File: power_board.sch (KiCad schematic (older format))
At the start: 27 parts, among them CON1 MICROUSB, J1 Conn_02x03_Odd_Even, J2 Conn_01x01, J3 Conn_01x01, J4 Conn_01x01, J5 Conn_01x01, SW1 SW_Push, U1 PCA9555PW, U2 ATMEGA328P-AU, U3 PCA9555PW, U4 FT232RL, Y1 Crystal

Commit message: Start MCU layout
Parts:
- added C1, C5, C6, C7, C9: 100nF, lsts-passives:C_0603, symbol Device:C
- renumbered C5 to C10, C1 to C2, C2 to C3, C3 to C4, C4 to C8
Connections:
- net +5V_SB: now also C1.2, C5.1, C6.1, C7.2
- net 5V_USB: now also C9.2
- net GND: now also C1.1, C5.2, C6.2, C7.1, C9.1
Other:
- moved on the sheet: C2, C8
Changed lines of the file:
@@
 	9550 3250 9450 3250
 $Comp
-L power:GND #PWR014
+L power:GND #PWR016
 U 1 1 5DC0D5DB
 P 9250 3400
-F 0 "#PWR014" H 9250 3150 50  0001 C CNN
+F 0 "#PWR016" H 9250 3150 50  0001 C CNN
 F 1 "GND" V 9255 3272 50  0000 R CNN
 F 2 "" H 9250 3400 50  0001 C CNN
@@
 	7650 1900 7800 1900
 $Comp
-L power:GND #PWR011
+L power:GND #PWR014
 U 1 1 5DC4811C
 P 7800 1300
-F 0 "#PWR011" H 7800 1050 50  0001 C CNN
+F 0 "#PWR014" H 7800 1050 50  0001 C CNN
 F 1 "GND" H 7805 1127 50  0000 C CNN
 F 2 "" H 7800 1300 50  0001 C CNN
@@
 	3750 1450 3600 1450
 $Comp
-L power:GND #PWR09
+L power:GND #PWR010
 U 1 1 5DC9272C
 P 4400 1550
-F 0 "#PWR09" H 4400 1300 50  0001 C CNN
+F 0 "#PWR010" H 4400 1300 50  0001 C CNN
 F 1 "GND" H 4405 1377 50  0000 C CNN
 F 2 "" H 4400 1550 50  0001 C CNN
@@
 MOSI
 $Comp
-L Device:C C4
+L Device:C C8
 U 1 1 5DCA5008
-P 7800 2200
-F 0 "C4" H 7915 2246 50  0000 L CNN
-F 1 "100nF" H 7915 2155 50  0000 L CNN
-F 2 "lsts-passives:C_0603" H 7838 2050 50  0001 C CNN
-F 3 "~" H 7800 2200 50  0001 C CNN
-	1    7800 2200
-	-1   0    0    1
-$EndComp
-$Comp
-L power:GND #PWR012
-U 1 1 5DCA65D2
-P 7800 2500
-F 0 "#PWR012" H 7800 2250 50  0001 C CNN
-F 1 "GND" H 7805 2327 50  0000 C CNN
-F 2 "" H 7800 2500 50  0001 C CNN
-F 3 "" H 7800 2500 50  0001 C CNN
-	1    7800 2500
-	1    0    0    -1
+P 7400 2700
+F 0 "C8" H 7515 2746 50  0000 L CNN
+F 1 "100nF" H 7515 2655 50  0000 L CNN
+F 2 "lsts-passives:C_0603" H 7438 2550 50  0001 C CNN
+F 3 "~" H 7400 2700 50  0001 C CNN
+	1    7400 2700
+	-1   0    0    1
 $EndComp
 Wire Wire Line
@@
 NoConn ~ 10250 2800
 $Comp
-L power:GND #PWR02
+L power:GND #PWR01
 U 1 1 5DC3EC2B
 P 950 3950
-F 0 "#PWR02" H 950 3700 50  0001 C CNN
+F 0 "#PWR01" H 950 3700 50  0001 C CNN
 F 1 "GND" H 955 3777 50  0000 C CNN
 F 2 "" H 950 3950 50  0001 C CNN
@@
 	3250 850  3400 850
 $Comp
-L Device:C C1
+L Device:C C2
 U 1 1 5DC4BEF5
-P 950 1100
-F 0 "C1" V 698 1100 50  0000 C CNN
-F 1 "100nF" V 789 1100 50  0000 C CNN
-F 2 "lsts-passives:C_0603" H 988 950 50  0001 C CNN
-F 3 "~" H 950 1100 50  0001 C CNN
-	1    950  1100
-	-1   0    0    1
-$EndComp
-$Comp
-L power:GND #PWR01
-U 1 1 5DC4DED9
-P 950 800
-F 0 "#PWR01" H 950 550 50  0001 C CNN
-F 1 "GND" V 955 672 50  0000 R CNN
-F 2 "" H 950 800 50  0001 C CNN
-F 3 "" H 950 800 50  0001 C CNN
-	1    950  800
-	-1   0    0    1
+P 3750 3200
+F 0 "C2" V 3498 3200 50  0000 C CNN
+F 1 "100nF" V 3589 3200 50  0000 C CNN
+F 2 "lsts-passives:C_0603" H 3788 3050 50  0001 C CNN
+F 3 "~" H 3750 3200 50  0001 C CNN
+	1    3750 3200
+	1    0    0    -1
 $EndComp
 Wire Wire Line
@@
 	2300 850  2150 850
 $Comp
-L power:GND #PWR04
+L power:GND #PWR03
 U 1 1 5DC6E12C
 P 2150 850
-F 0 "#PWR04" H 2150 600 50  0001 C CNN
+F 0 "#PWR03" H 2150 600 50  0001 C CNN
 F 1 "GND" H 2155 677 50  0000 C CNN
 F 2 "" H 2150 850 50  0001 C CNN
@@
 $EndComp
 $Comp
-L Device:C C2
+L Device:C C3
 U 1 1 5DC9A9C9
 P 3800 2000
-F 0 "C2" V 3548 2000 50  0000 C CNN
+F 0 "C3" V 3548 2000 50  0000 C CNN
 F 1 "22nF" V 3639 2000 50  0000 C CNN
 F 2 "lsts-passives:C_0603" H 3838 1850 50  0001 C CNN
@@
 $EndComp
 $Comp
-L Device:C C3
+L Device:C C4
 U 1 1 5DC9B617
 P 3800 2300
-F 0 "C3" V 3960 2300 50  0000 C CNN
+F 0 "C4" V 3960 2300 50  0000 C CNN
 F 1 "22nF" V 4051 2300 50  0000 C CNN
 F 2 "lsts-passives:C_0603" H 3838 2150 50  0001 C CNN
@@
 Wire Wire Line
 	3950 2300 4150 2300
-Text Label 800  1350 2    50   ~ 0
+Text Label 950  1200 1    50   ~ 0
 +5V_SB
-Wire Wire Line
-	950  950  950  800
-Wire Wire Line
-	950  1350 800  1350
-Connection ~ 950  1350
-Wire Wire Line
-	950  1350 950  1250
 $Comp
 L lsts-conn:MICROUSB CON1
@@
 	1750 7050 1750 7150
 $Comp
-L power:GND #PWR03
+L power:GND #PWR02
 U 1 1 5E1B9B28
 P 1750 7150
-F 0 "#PWR03" H 1750 6900 50  0001 C CNN
+F 0 "#PWR02" H 1750 6900 50  0001 C CNN
 F 1 "GND" H 1755 6977 50  0000 C CNN
 F 2 "" H 1750 7150 50  0001 C CNN
@@
 	4250 7050 4250 7150
 $Comp
-L power:GND #PWR08
+L power:GND #PWR09
 U 1 1 5E1C2465
 P 4250 7150
-F 0 "#PWR08" H 4250 6900 50  0001 C CNN
+F 0 "#PWR09" H 4250 6900 50  0001 C CNN
 F 1 "GND" H 4255 6977 50  0000 C CNN
 F 2 "" H 4250 7150 50  0001 C CNN
@@
 	9350 1100 9350 950
 $Comp
-L power:GND #PWR013
+L power:GND #PWR015
 U 1 1 5DC6C013
 P 8550 750
-F 0 "#PWR013" H 8550 500 50  0001 C CNN
+F 0 "#PWR015" H 8550 500 50  0001 C CNN
 F 1 "GND" H 8555 577 50  0000 C CNN
 F 2 "" H 8550 750 50  0001 C CNN
@@
 	8650 1400 8550 1400
 $Comp
-L Device:C C5
+L Device:C C10
 U 1 1 5DC6AA97
 P 8550 1100
-F 0 "C5" H 8665 1146 50  0000 L CNN
+F 0 "C10" H 8665 1146 50  0000 L CNN
 F 1 "100nF" H 8665 1055 50  0000 L CNN
 F 2 "lsts-passives:C_0603" H 8588 950 50  0001 C CNN
@@
 Text Label 4400 1250 0    50   ~ 0
 +5V_SB
-Wire Wire Line
-	7800 1900 7800 2050
-Wire Wire Line
-	7800 2350 7800 2500
 Text Label 7800 1900 0    50   ~ 0
 5V_USB
@@
 $EndComp
 $Comp
-L power:GND #PWR010
+L power:GND #PWR012
 U 1 1 5E29E574
 P 6700 7500
-F 0 "#PWR010" H 6700 7250 50  0001 C CNN
+F 0 "#PWR012" H 6700 7250 50  0001 C CNN
 F 1 "GND" H 6705 7327 50  0000 C CNN
 F 2 "" H 6700 7500 50  0001 C CNN
@@
 	950  3600 950  3700
 Connection ~ 950  3700
-Wire Wire Line
-	950  1500 950  1350
 Wire Wire Line
 	950  1600 950  1500
@@
 NoConn ~ 4750 6700
 NoConn ~ 4750 6800
+Wire Wire Line
+	950  1200 950  1500
+$Comp
+L Device:C C5
+U 1 1 5E48DB47
+P 4150 3200
+F 0 "C5" V 3898 3200 50  0000 C CNN
+F 1 "100nF" V 3989 3200 50  0000 C CNN
+F 2 "lsts-passives:C_0603" H 4188 3050 50  0001 C CNN
+F 3 "~" H 4150 3200 50  0001 C CNN
+	1    4150 3200
+	1    0    0    -1
+$EndComp
+$Comp
+L power:GND #PWR08
+U 1 1 5E48DB4D
+P 4150 3500
+F 0 "#PWR08" H 4150 3250 50  0001 C CNN
+F 1 "GND" V 4155 3372 50  0000 R CNN
+F 2 "" H 4150 3500 50  0001 C CNN
+F 3 "" H 4150 3500 50  0001 C CNN
+	1    4150 3500
+	1    0    0    -1
+$EndComp
+Wire Wire Line
+	4150 3350 4150 3500
+Wire Wire Line
+	4150 2900 4150 3050
+$Comp
+L Device:C C6
+U 1 1 5E499A74
+P 4550 3200
+F 0 "C6" V 4298 3200 50  0000 C CNN
+F 1 "100nF" V 4389 3200 50  0000 C CNN
+F 2 "lsts-passives:C_0603" H 4588 3050 50  0001 C CNN
+F 3 "~" H 4550 3200 50  0001 C CNN
+	1    4550 3200
+	1    0    0    -1
+$EndComp
+Wire Wire Line
+	3750 3350 4150 3350
+Connection ~ 4150 3350
+Wire Wire Line
+	4150 3350 4550 3350
+Wire Wire Line
+	3750 3050 4150 3050
+Connection ~ 4150 3050
+Wire Wire Line
+	4150 3050 4550 3050
+Text Label 4150 2900 1    50   ~ 0
++5V_SB
+$Comp
+L Device:C C9
+U 1 1 5E51421A
+P 7800 2700
+F 0 "C9" H 7685 2654 50  0000 R CNN
+F 1 "100nF" H 7685 2745 50  0000 R CNN
+F 2 "lsts-passives:C_0603" H 7838 2550 50  0001 C CNN
+F 3 "~" H 7800 2700 50  0001 C CNN
+	1    7800 2700
+	-1   0    0    1
+$EndComp
+$Comp
+L power:GND #PWR013
+U 1 1 5E514220
+P 7600 3000
+F 0 "#PWR013" H 7600 2750 50  0001 C CNN
+F 1 "GND" H 7605 2827 50  0000 C CNN
+F 2 "" H 7600 3000 50  0001 C CNN
+F 3 "" H 7600 3000 50  0001 C CNN
+	1    7600 3000
+	1    0    0    -1
+$EndComp
+Wire Wire Line
+	7400 2550 7600 2550
+Wire Wire Line
+	7400 2850 7600 2850
+Wire Wire Line
+	7600 3000 7600 2850
+Connection ~ 7600 2850
+Wire Wire Line
+	7600 2850 7800 2850
+Wire Wire Line
+	7600 2550 7600 2400
+Connection ~ 7600 2550
+Wire Wire Line
+	7600 2550 7800 2550
+Text Label 7600 2400 1    50   ~ 0
+5V_USB
+Wire Wire Line
+	1750 4800 1900 4800
+Connection ~ 1750 4800
+$Comp
+L Device:C C1
+U 1 1 5E59E313
+P 2050 4800
+F 0 "C1" V 1798 4800 50  0000 C CNN
+F 1 "100nF" V 1889 4800 50  0000 C CNN
+F 2 "lsts-passives:C_0603" H 2088 4650 50  0001 C CNN
+F 3 "~" H 2050 4800 50  0001 C CNN
+	1    2050 4800
+	0    1    1    0
+$EndComp
+Wire Wire Line
+	2200 4800 2350 4800
+$Comp
+L power:GND #PWR04
+U 1 1 5E5AD9E4
+P 2350 4800
+F 0 "#PWR04" H 2350 4550 50  0001 C CNN
+F 1 "GND" H 2355 4627 50  0000 C CNN
+F 2 "" H 2350 4800 50  0001 C CNN
+F 3 "" H 2350 4800 50  0001 C CNN
+	1    2350 4800
+	0    -1   -1   0
+$EndComp
+Wire Wire Line
+	4250 4800 4400 4800
+$Comp
+L Device:C C7
+U 1 1 5E5B075C
+P 4550 4800
+F 0 "C7" V 4298 4800 50  0000 C CNN
+F 1 "100nF" V 4389 4800 50  0000 C CNN
+F 2 "lsts-passives:C_0603" H 4588 4650 50  0001 C CNN
+F 3 "~" H 4550 4800 50  0001 C CNN
+	1    4550 4800
+	0    1    1    0
+$EndComp
+Wire Wire Line
+	4700 4800 4850 4800
+$Comp
+L power:GND #PWR011
+U 1 1 5E5B0763
+P 4850 4800
+F 0 "#PWR011" H 4850 4550 50  0001 C CNN
+F 1 "GND" H 4855 4627 50  0000 C CNN
+F 2 "" H 4850 4800 50  0001 C CNN
+F 3 "" H 4850 4800 50  0001 C CNN
+	1    4850 4800
+	0    -1   -1   0
+$EndComp
 $EndSCHEMATC

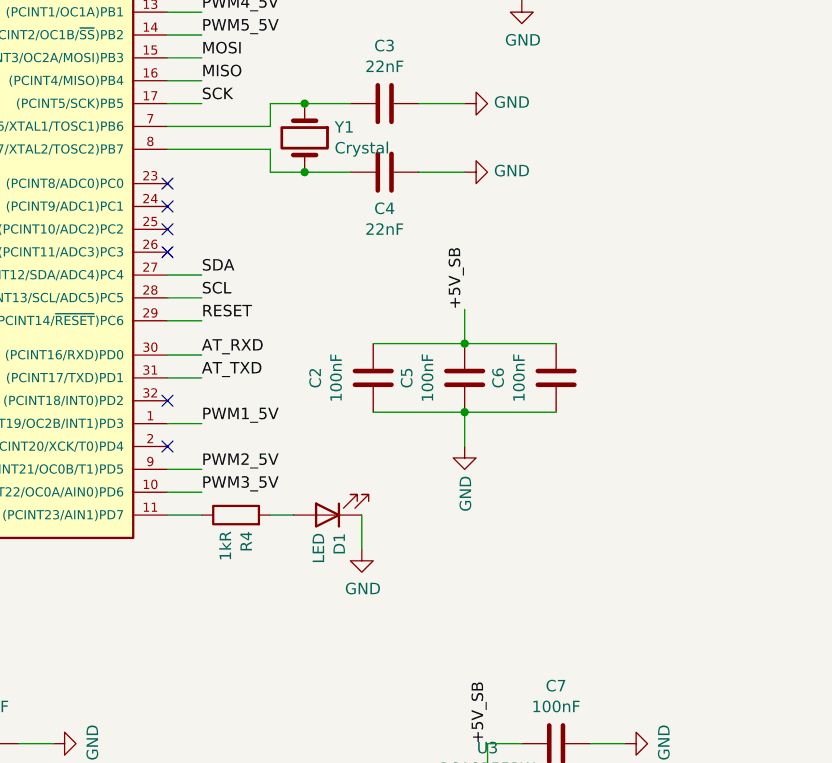
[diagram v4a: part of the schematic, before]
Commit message: Initial MCU positioning. Reassign LED.
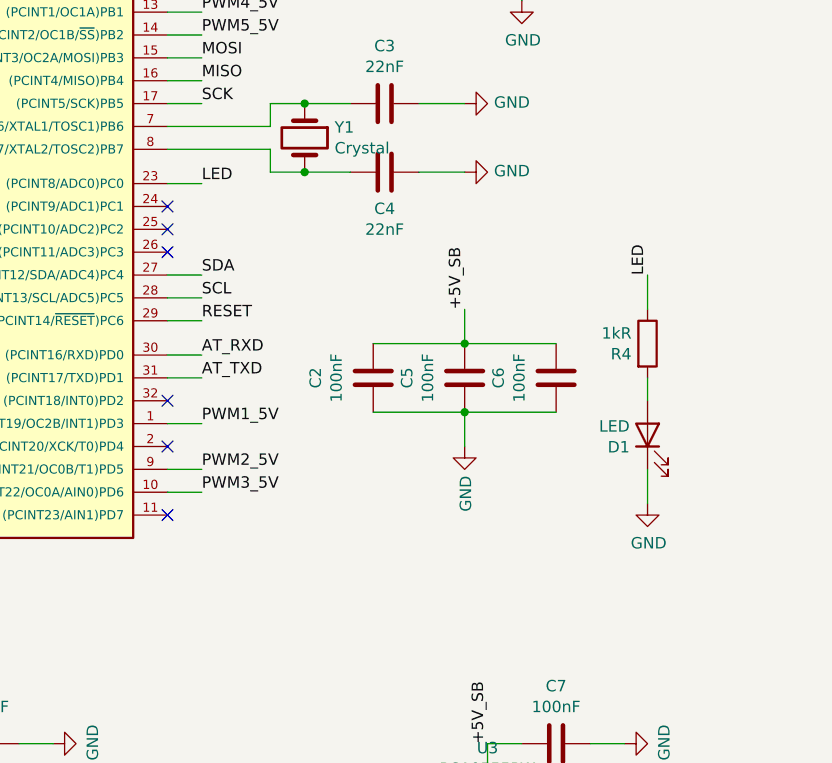
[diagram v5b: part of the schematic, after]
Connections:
- net at U2.11 ((PCINT23/AIN1)PD7): no longer R4.1
- net LED: now reaches U2.23 ((PCINT8/ADC0)PC0)
- net LED: now also R4.1
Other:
- moved on the sheet: D1, R4
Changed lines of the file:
@@
 NoConn ~ 2850 2550
 NoConn ~ 2850 2450
-NoConn ~ 2850 2350
 $Comp
 L Connector_Generic:Conn_01x01 J5
@@
 L Device:LED D1
 U 1 1 5E321428
-P 3550 3800
-F 0 "D1" V 3497 3878 50  0000 L CNN
-F 1 "LED" V 3588 3878 50  0000 L CNN
-F 2 "lsts-discretes:LED_0603" H 3550 3800 50  0001 C CNN
-F 3 "~" H 3550 3800 50  0001 C CNN
-	1    3550 3800
-	-1   0    0    1
-$EndComp
-Wire Wire Line
-	3400 3800 3300 3800
+P 4950 3450
+F 0 "D1" V 4897 3528 50  0000 L CNN
+F 1 "LED" V 4988 3528 50  0000 L CNN
+F 2 "lsts-discretes:LED_0603" H 4950 3450 50  0001 C CNN
+F 3 "~" H 4950 3450 50  0001 C CNN
+	1    4950 3450
+	0    -1   -1   0
+$EndComp
+Wire Wire Line
+	4950 3300 4950 3200
 $Comp
 L Device:R R4
 U 1 1 5E32142F
-P 3150 3800
-F 0 "R4" H 3080 3754 50  0000 R CNN
-F 1 "1kR" H 3080 3845 50  0000 R CNN
-F 2 "lsts-passives:R_0603" V 3080 3800 50  0001 C CNN
-F 3 "~" H 3150 3800 50  0001 C CNN
-	1    3150 3800
-	0    -1   -1   0
-$EndComp
-Wire Wire Line
-	2850 3800 3000 3800
+P 4950 3050
+F 0 "R4" H 4880 3004 50  0000 R CNN
+F 1 "1kR" H 4880 3095 50  0000 R CNN
+F 2 "lsts-passives:R_0603" V 4880 3050 50  0001 C CNN
+F 3 "~" H 4950 3050 50  0001 C CNN
+	1    4950 3050
+	1    0    0    -1
+$EndComp
+Wire Wire Line
+	4950 2750 4950 2900
 $Comp
 L power:GND #PWR05
 U 1 1 5E35F179
-P 3700 3950
-F 0 "#PWR05" H 3700 3700 50  0001 C CNN
-F 1 "GND" H 3705 3777 50  0000 C CNN
-F 2 "" H 3700 3950 50  0001 C CNN
-F 3 "" H 3700 3950 50  0001 C CNN
-	1    3700 3950
-	1    0    0    -1
-$EndComp
-Wire Wire Line
-	3700 3800 3700 3950
+P 4950 3750
+F 0 "#PWR05" H 4950 3500 50  0001 C CNN
+F 1 "GND" H 4955 3577 50  0000 C CNN
+F 2 "" H 4950 3750 50  0001 C CNN
+F 3 "" H 4950 3750 50  0001 C CNN
+	1    4950 3750
+	1    0    0    -1
+$EndComp
+Wire Wire Line
+	4950 3600 4950 3750
 Wire Wire Line
 	3750 6800 3750 7050
@@
 	0    -1   -1   0
 $EndComp
+NoConn ~ 2850 3800
+Wire Wire Line
+	2850 2350 3000 2350
+Text Label 3000 2350 0    50   ~ 0
+LED
+Text Label 4950 2750 1    50   ~ 0
+LED
 $EndSCHEMATC

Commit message: Stash
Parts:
- removed J4: Conn_01x01, lsts-mecanical:MountingHole_3.5mm_Pad, symbol Connector_Generic:Conn_01x01
- renumbered J5 to J4, R5 to R4, R4 to R5
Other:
- moved on the sheet: J2, J3
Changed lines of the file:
@@
 	3750 1450 3600 1450
 $Comp
-L power:GND #PWR010
+L power:GND #PWR09
 U 1 1 5DC9272C
 P 4400 1550
-F 0 "#PWR010" H 4400 1300 50  0001 C CNN
+F 0 "#PWR09" H 4400 1300 50  0001 C CNN
 F 1 "GND" H 4405 1377 50  0000 C CNN
 F 2 "" H 4400 1550 50  0001 C CNN
@@
 $EndComp
 $Comp
-L power:GND #PWR06
+L power:GND #PWR05
 U 1 1 5DC9BC40
 P 4150 2000
-F 0 "#PWR06" H 4150 1750 50  0001 C CNN
+F 0 "#PWR05" H 4150 1750 50  0001 C CNN
 F 1 "GND" V 4155 1872 50  0000 R CNN
 F 2 "" H 4150 2000 50  0001 C CNN
@@
 $EndComp
 $Comp
-L power:GND #PWR07
+L power:GND #PWR06
 U 1 1 5DC9C15F
 P 4150 2300
-F 0 "#PWR07" H 4150 2050 50  0001 C CNN
+F 0 "#PWR06" H 4150 2050 50  0001 C CNN
 F 1 "GND" V 4155 2172 50  0000 R CNN
 F 2 "" H 4150 2300 50  0001 C CNN
@@
 	4250 7050 4250 7150
 $Comp
-L power:GND #PWR09
+L power:GND #PWR08
 U 1 1 5E1C2465
 P 4250 7150
-F 0 "#PWR09" H 4250 6900 50  0001 C CNN
+F 0 "#PWR08" H 4250 6900 50  0001 C CNN
 F 1 "GND" H 4255 6977 50  0000 C CNN
 F 2 "" H 4250 7150 50  0001 C CNN
@@
 RLY5_EN
 $Comp
-L Device:R R5
+L Device:R R4
 U 1 1 5E1910A1
 P 3750 6400
-F 0 "R5" H 3819 6354 50  0000 L CNN
+F 0 "R4" H 3819 6354 50  0000 L CNN
 F 1 "10kR" H 3819 6445 50  0000 L CNN
 F 2 "lsts-passives:R_0603" V 3680 6400 50  0001 C CNN
@@
 NoConn ~ 2850 2450
 $Comp
-L Connector_Generic:Conn_01x01 J5
+L Connector_Generic:Conn_01x01 J4
 U 1 1 5E28827E
 P 6400 7400
-F 0 "J5" H 6550 7350 50  0000 C CNN
+F 0 "J4" H 6550 7350 50  0000 C CNN
 F 1 "Conn_01x01" H 6750 7450 50  0000 C CNN
 F 2 "lsts-mecanical:MountingHole_3.5mm_Pad" H 6400 7400 50  0001 C CNN
@@
 $EndComp
 $Comp
-L Connector_Generic:Conn_01x01 J4
-U 1 1 5E28A83A
+L Connector_Generic:Conn_01x01 J3
+U 1 1 5E29484D
 P 6400 7200
-F 0 "J4" H 6550 7150 50  0000 C CNN
+F 0 "J3" H 6550 7150 50  0000 C CNN
 F 1 "Conn_01x01" H 6750 7250 50  0000 C CNN
 F 2 "lsts-mecanical:MountingHole_3.5mm_Pad" H 6400 7200 50  0001 C CNN
 F 3 "~" H 6400 7200 50  0001 C CNN
 	1    6400 7200
-	-1   0    0    1
-$EndComp
-$Comp
-L Connector_Generic:Conn_01x01 J3
-U 1 1 5E29484D
-P 6400 7000
-F 0 "J3" H 6550 6950 50  0000 C CNN
-F 1 "Conn_01x01" H 6750 7050 50  0000 C CNN
-F 2 "lsts-mecanical:MountingHole_3.5mm_Pad" H 6400 7000 50  0001 C CNN
-F 3 "~" H 6400 7000 50  0001 C CNN
-	1    6400 7000
-	-1   0    0    1
-$EndComp
-$Comp
-L Connector_Generic:Conn_01x01 J2
-U 1 1 5E294857
-P 6400 6800
-F 0 "J2" H 6550 6750 50  0000 C CNN
-F 1 "Conn_01x01" H 6750 6850 50  0000 C CNN
-F 2 "lsts-mecanical:MountingHole_3.5mm_Pad" H 6400 6800 50  0001 C CNN
-F 3 "~" H 6400 6800 50  0001 C CNN
-	1    6400 6800
 	-1   0    0    1
 $EndComp
@@
 $EndComp
 Wire Wire Line
-	6600 6800 6700 6800
-Wire Wire Line
-	6700 6800 6700 7000
-Wire Wire Line
 	6600 7400 6700 7400
 Connection ~ 6700 7400
@@
 	6700 7400 6700 7500
 Wire Wire Line
-	6600 7200 6700 7200
-Connection ~ 6700 7200
-Wire Wire Line
-	6700 7200 6700 7400
-Wire Wire Line
 	6600 7000 6700 7000
-Connection ~ 6700 7000
-Wire Wire Line
-	6700 7000 6700 7200
 Connection ~ 950  1600
 Wire Wire Line
@@
 	4950 3300 4950 3200
 $Comp
-L Device:R R4
+L Device:R R5
 U 1 1 5E32142F
 P 4950 3050
-F 0 "R4" H 4880 3004 50  0000 R CNN
+F 0 "R5" H 4880 3004 50  0000 R CNN
 F 1 "1kR" H 4880 3095 50  0000 R CNN
 F 2 "lsts-passives:R_0603" V 4880 3050 50  0001 C CNN
@@
 	4950 2750 4950 2900
 $Comp
-L power:GND #PWR05
+L power:GND #PWR011
 U 1 1 5E35F179
 P 4950 3750
-F 0 "#PWR05" H 4950 3500 50  0001 C CNN
+F 0 "#PWR011" H 4950 3500 50  0001 C CNN
 F 1 "GND" H 4955 3577 50  0000 C CNN
 F 2 "" H 4950 3750 50  0001 C CNN
@@
 $EndComp
 $Comp
-L power:GND #PWR08
+L power:GND #PWR07
 U 1 1 5E48DB4D
 P 4150 3500
-F 0 "#PWR08" H 4150 3250 50  0001 C CNN
+F 0 "#PWR07" H 4150 3250 50  0001 C CNN
 F 1 "GND" V 4155 3372 50  0000 R CNN
 F 2 "" H 4150 3500 50  0001 C CNN
@@
 	4700 4800 4850 4800
 $Comp
-L power:GND #PWR011
+L power:GND #PWR010
 U 1 1 5E5B0763
 P 4850 4800
-F 0 "#PWR011" H 4850 4550 50  0001 C CNN
+F 0 "#PWR010" H 4850 4550 50  0001 C CNN
 F 1 "GND" H 4855 4627 50  0000 C CNN
 F 2 "" H 4850 4800 50  0001 C CNN
@@
 Text Label 4950 2750 1    50   ~ 0
 LED
+$Comp
+L Connector_Generic:Conn_01x01 J2
+U 1 1 5E294857
+P 6400 7000
+F 0 "J2" H 6550 6950 50  0000 C CNN
+F 1 "Conn_01x01" H 6750 7050 50  0000 C CNN
+F 2 "lsts-mecanical:MountingHole_3.5mm_Pad" H 6400 7000 50  0001 C CNN
+F 3 "~" H 6400 7000 50  0001 C CNN
+	1    6400 7000
+	-1   0    0    1
+$EndComp
+Wire Wire Line
+	6700 7000 6700 7200
+Wire Wire Line
+	6600 7200 6700 7200
+Connection ~ 6700 7200
+Wire Wire Line
+	6700 7200 6700 7400
 $EndSCHEMATC
